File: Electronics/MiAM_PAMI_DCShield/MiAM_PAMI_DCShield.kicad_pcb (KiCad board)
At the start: 2 copper layers, 43.7 x 54.2 mm, 11 parts, among them U1 ESP32-DEVKIT-V1, U4 TB6612FNG

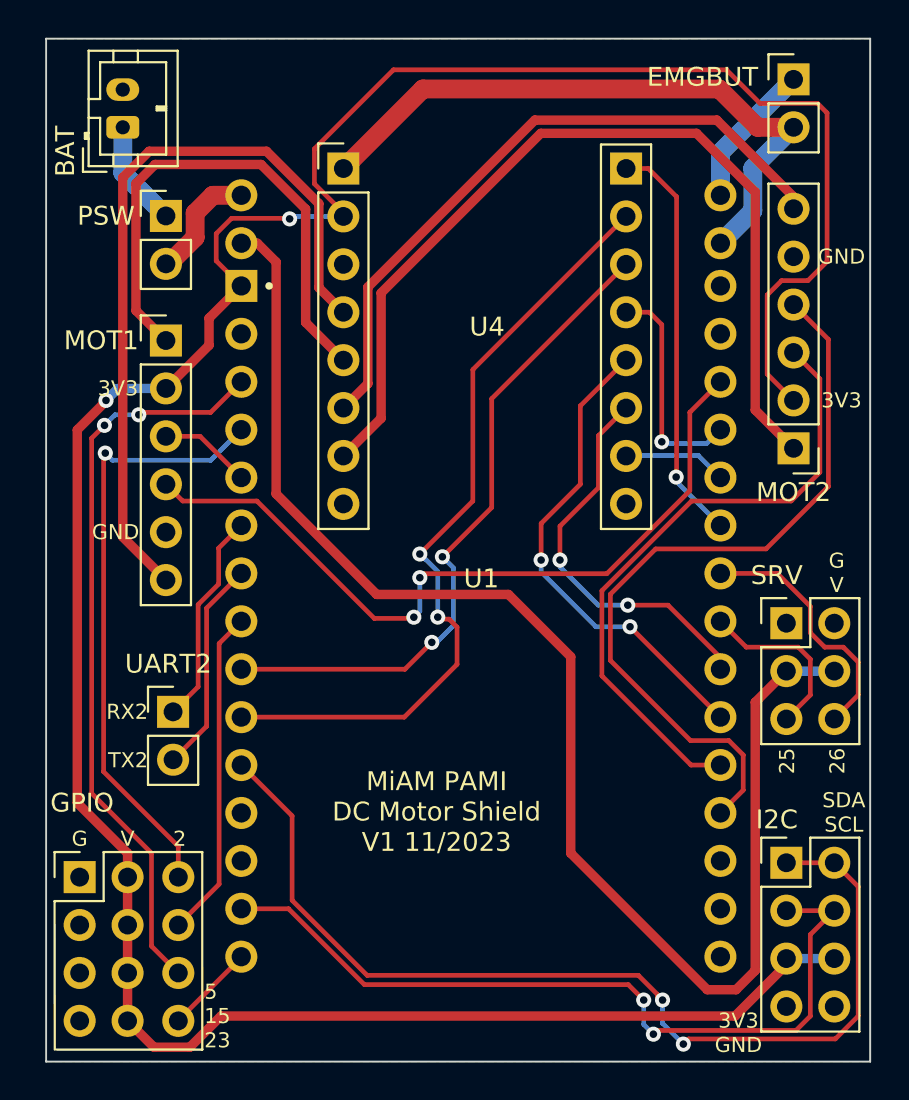
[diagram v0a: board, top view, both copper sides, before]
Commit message: Fix shield footprint
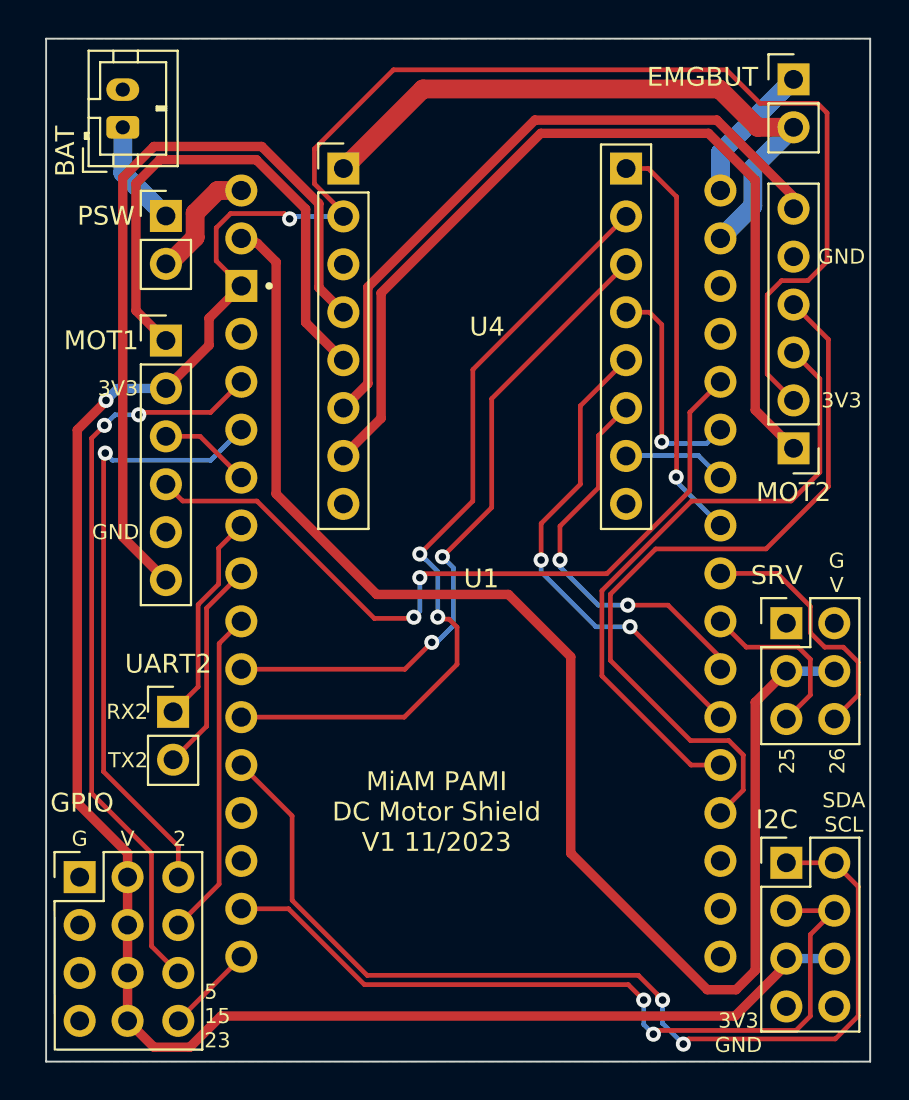
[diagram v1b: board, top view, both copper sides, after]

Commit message: Faster DC
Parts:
- moved MOT1 12.6 mm to (53.8, 75.1), turned to 180 degrees
- renumbered BAT to BAT1, EMGBUT to EMGBUT1, GPIO to GPIO1, I2C to I2C1, PSW to PSW1, SRV to SRV1
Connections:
- MOT1 pad 1: /2Y -> /1Y
- MOT1 pad 6: /1Y -> /2Y
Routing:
- net /SDA: track 54.2 -> 37.2 mm, vias 2 -> 1
- net /SCL: track 42.7 -> 35.1 mm, vias 2 -> 1
- net +3V3: track 148.2 -> 155.7 mm, vias 2 -> 4
- net /ENCODER_A1: track 41.0 -> 44.2 mm
- net /1A: track 35.6 -> 32.8 mm
- net /2A: track 42.0 -> 40.0 mm
- net /ENCODER_B1: track 4.90 -> 3.96 mm
